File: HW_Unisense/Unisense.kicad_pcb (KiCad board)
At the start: 2 copper layers, 72 parts, among them J2 SW1, J3 SW2, J4 GeigerCounter, J5 WS2812, J6 LED1, J7 LED2, J8 LED3, P1 SM02B-NSHSS-TB(LF)(SN), Q1 BSN20, Q2 BSN20, Q3 BSN20, Q4 BSN20, Q5 AO3400A, Q6 AO3400A, Q7 AO3400A, Q8 IRLML6402TRPBF, SW1 K2-1102SP-C4SC-04, SW2 K2-1102SP-C4SC-04, SW3 K2-1102SP-C4SC-04, SW4 K2-1102SP-C4SC-04, U1 ESP32-S3-WROOM-1(N8R2), U2 S4B-PH-SM4-K-TB(LF)(SN), U3 LD1117S33TR, U4 TMP112xxDRL, U5 BME280, U6 BMP280, U7 VEML6040A3OG, U8 MCP73831T-2ATI/OT, U9 MAX17048G+T10

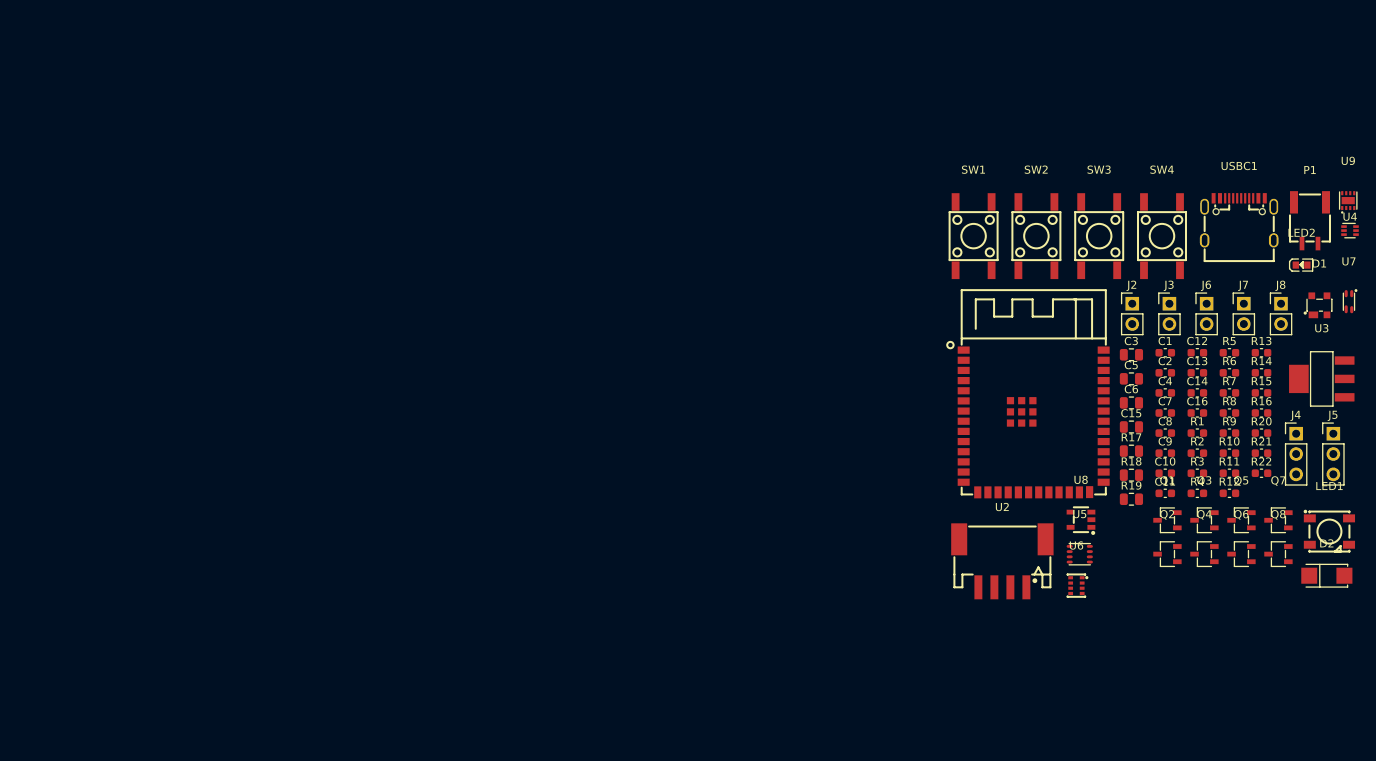
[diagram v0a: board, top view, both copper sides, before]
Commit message: add more sensors and arrange on multiple pages
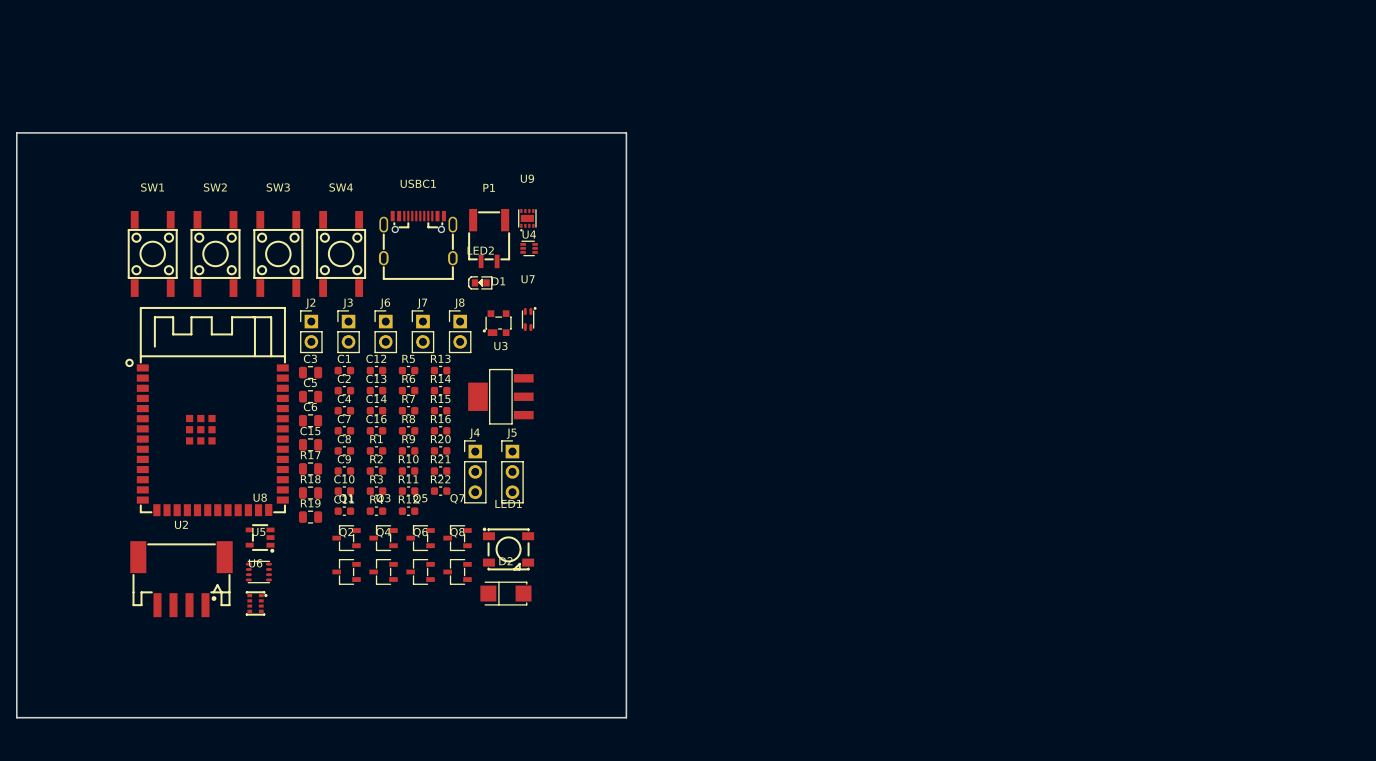
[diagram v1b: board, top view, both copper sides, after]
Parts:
- moved C1 102.6 mm to (150.3, 89.3)
- moved C10 102.6 mm to (150.3, 104.4)
- moved C11 102.6 mm to (150.3, 106.9)
- moved C12 102.6 mm to (154.4, 89.3)
- moved C13 102.6 mm to (154.4, 91.8)
- moved C14 102.6 mm to (154.4, 94.3)
- moved C16 102.6 mm to (154.4, 96.8)
- moved C2 102.6 mm to (150.3, 91.8)
- moved C4 102.6 mm to (150.3, 94.3)
- moved C7 102.6 mm to (150.3, 96.8)
- moved C8 102.6 mm to (150.3, 99.3)
- moved C9 102.6 mm to (150.3, 101.9)
- moved D1 102.6 mm to (169.6, 83.4)
- moved J2 102.6 mm to (146.2, 83.2)
- moved J5 102.6 mm to (171.4, 99.4)
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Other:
- board outline added: 76.2 x 73.1 mm

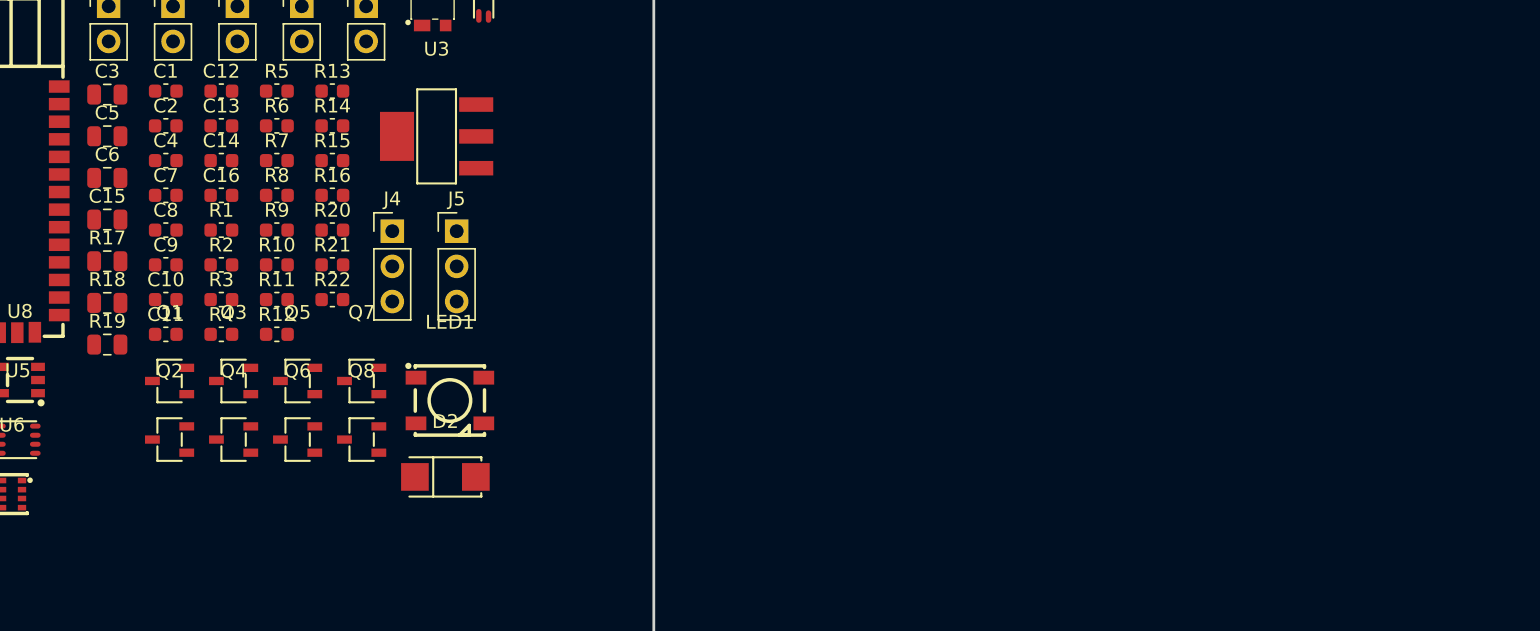
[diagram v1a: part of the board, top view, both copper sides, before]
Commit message: change power net names, as V8 handles them like a champ
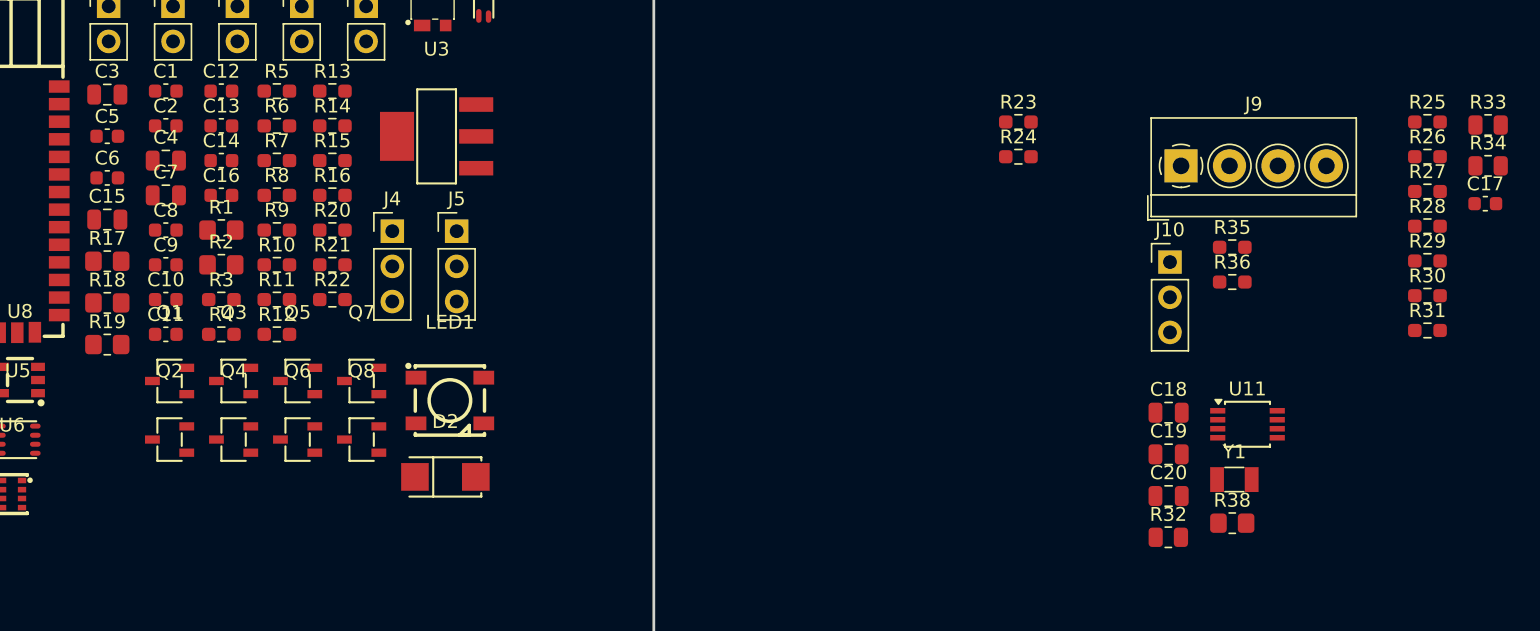
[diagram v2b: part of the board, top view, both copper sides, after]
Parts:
- added C17: 100n, Capacitor_SMD:C_0603_1608Metric, F.Cu at (245.7, 97.4)
- added C18: 1uF, Capacitor_SMD:C_0805_2012Metric, F.Cu at (222.8, 112.5)
- added C19: 100nF, Capacitor_SMD:C_0805_2012Metric, F.Cu at (222.8, 115.5)
- added C20: 100nF, Capacitor_SMD:C_0805_2012Metric, F.Cu at (222.8, 118.6)
- added J10: OneWire, Connector_PinHeader_2.54mm:PinHeader_1x03_P2.54mm_Vertical, F.Cu at (222.9, 101.7)
- added J9: RS485, TerminalBlock_4Ucon:TerminalBlock_4Ucon_1x04_P3.50mm_Horizontal, F.Cu at (223.7, 94.7)
- added R23: 100k, Resistor_SMD:R_0603_1608Metric_Pad0.98x0.95mm_HandSolder, F.Cu at (211.9, 91.5)
- added R24: 100k, Resistor_SMD:R_0603_1608Metric_Pad0.98x0.95mm_HandSolder, F.Cu at (211.9, 94.0)
- added R25: 100k, Resistor_SMD:R_0603_1608Metric_Pad0.98x0.95mm_HandSolder, F.Cu at (241.5, 91.5)
- added R26: 1k, Resistor_SMD:R_0603_1608Metric_Pad0.98x0.95mm_HandSolder, F.Cu at (241.5, 94.0)
- added R27: 1k, Resistor_SMD:R_0603_1608Metric_Pad0.98x0.95mm_HandSolder, F.Cu at (241.5, 96.6)
- added R28: 1k, Resistor_SMD:R_0603_1608Metric_Pad0.98x0.95mm_HandSolder, F.Cu at (241.5, 99.1)
- added R29: 1k, Resistor_SMD:R_0603_1608Metric_Pad0.98x0.95mm_HandSolder, F.Cu at (241.5, 101.6)
- added R30: 1k, Resistor_SMD:R_0603_1608Metric_Pad0.98x0.95mm_HandSolder, F.Cu at (241.5, 104.1)
- added R31: 1k, Resistor_SMD:R_0603_1608Metric_Pad0.98x0.95mm_HandSolder, F.Cu at (241.5, 106.6)
- added R32: 10k, Resistor_SMD:R_0805_2012Metric, F.Cu at (222.8, 121.5)
- added R33: 10k, Resistor_SMD:R_0805_2012Metric, F.Cu at (245.9, 91.8)
- added R34: 10k, Resistor_SMD:R_0805_2012Metric, F.Cu at (245.9, 94.7)
- added R35: 33k, Resistor_SMD:R_0603_1608Metric_Pad0.98x0.95mm_HandSolder, F.Cu at (227.4, 100.6)
- added R36: 1k, Resistor_SMD:R_0603_1608Metric_Pad0.98x0.95mm_HandSolder, F.Cu at (227.4, 103.1)
- added R38: 4R7, Resistor_SMD:R_0805_2012Metric_Pad1.20x1.40mm_HandSolder, F.Cu at (227.4, 120.5)
- added U11: PCF85263ATT, Package_SO:TSSOP-8_3x3mm_P0.65mm, F.Cu at (228.5, 113.4)
- added Y1: Crystal, Crystal:Crystal_SMD_3215-2Pin_3.2x1.5mm, F.Cu at (227.5, 117.4)
- C4, C7: value 100n -> 10u; footprint Capacitor_SMD:C_0603_1608Metric -> Capacitor_SMD:C_0805_2012Metric
- C5, C6: value 10u -> 100n; footprint Capacitor_SMD:C_0805_2012Metric -> Capacitor_SMD:C_0603_1608Metric
- R1, R2: footprint Capacitor_SMD:C_0603_1608Metric -> Resistor_SMD:R_0805_2012Metric_Pad1.20x1.40mm_HandSolder
- R10, R11, R13, R14, R20, R21, R22, R3, R4, R5, R6, R7, R8, R9: footprint Capacitor_SMD:C_0603_1608Metric -> Resistor_SMD:R_0603_1608Metric_Pad0.98x0.95mm_HandSolder
- R12, R16: value 1k -> 100k; footprint Capacitor_SMD:C_0603_1608Metric -> Resistor_SMD:R_0603_1608Metric_Pad0.98x0.95mm_HandSolder
- R15: value 1k -> 21k; footprint Capacitor_SMD:C_0603_1608Metric -> Resistor_SMD:R_0603_1608Metric_Pad0.98x0.95mm_HandSolder
- R17, R18, R19: footprint Capacitor_SMD:C_0805_2012Metric -> Resistor_SMD:R_0805_2012Metric_Pad1.20x1.40mm_HandSolder
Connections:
- C10 pad 1: SDA -> Net-(U6-VDD)
- C12 pad 1: Net-(U6-VDD) -> +VSW
- C13 pad 1: SDA -> +VSW
- C14 pad 2: SDA -> +VSW
- C2 pad 1: SDA -> +3.3V
- C3 pad 1: SDA -> +3.3V
- C6 pad 1: SDA -> +3.3V
- C7 pad 1: SDA -> +3.3V
- C8 pad 1: +5V -> Vdrive
- C9 pad 1: SDA -> +VSW
- J4 pad 2: +5V -> Vdrive
- J5 pad 1: +5V -> Vdrive
- LED1 pad 1: +5V -> Vdrive
- Q1 pad 1: SDA -> +VSW
- Q2 pad 1: SDA -> +VSW
- Q2 pad 2: Net-(Q2-S) -> SDA
- Q3 pad 1: SDA -> +VSW
- Q4 pad 1: SDA -> +VSW
- R10 pad 2: SDA -> +VSW
- R11 pad 2: +5V -> Vdrive
- R12 pad 1: SDA -> +3.3V
- R13 pad 2: SDA -> +VSW
- R14 pad 2: +5V -> Vdrive
- R16 pad 1: SDA -> +3.3V
- R17 pad 2: +5V -> Vdrive
- R18 pad 2: +5V -> Vdrive
- R19 pad 2: +5V -> Vdrive
- R3 pad 2: Net-(USBC1-CC1) -> Net-(USBC1-CC2)
- R4 pad 2: Net-(USBC1-CC2) -> Net-(USBC1-CC1)
- R5 pad 2: SDA -> +3.3V
- R6 pad 1: Net-(Q2-S) -> SCL
- R6 pad 2: SDA -> +VSW
- R7 pad 1: Net-(Q2-D) -> SDA
- R7 pad 2: Net-(JP1-C) -> +VSW
- R9 pad 1: SCL -> Net-(Q2-D)
- R9 pad 2: SDA -> Net-(JP1-C)
- U1 pad 10: unconnected-(U1-IO17-Pad10) -> RS485_TX
- U1 pad 11: unconnected-(U1-IO18-Pad11) -> RS485_RX
- U1 pad 12: unconnected-(U1-IO8-Pad12) -> ~{General_Reset}
- U1 pad 16: unconnected-(U1-IO46-Pad16) -> LED1
- U1 pad 17: WS2812_Data2 -> LED2
- U1 pad 18: LED1 -> LED3
- U1 pad 19: LED2 -> TFT_CS
- U1 pad 2: SDA -> +3.3V
- U1 pad 20: LED3 -> SPI0_MISO
- U1 pad 21: unconnected-(U1-IO13-Pad21) -> SPI0_MOSI
- U1 pad 22: unconnected-(U1-IO14-Pad22) -> SPI0_CLK
- U1 pad 31: unconnected-(U1-IO38-Pad31) -> OnWire_Data
- U1 pad 32: unconnected-(U1-IO39-Pad32) -> EnPower
- U1 pad 4: WS2812_Data1 -> unconnected-(U1-IO4-Pad4)
- U1 pad 6: unconnected-(U1-IO6-Pad6) -> RS485_EN
- U1 pad 7: unconnected-(U1-IO7-Pad7) -> WS2812_Data1
- U1 pad 8: unconnected-(U1-IO15-Pad8) -> WS2812_Data2
- U1 pad 9: unconnected-(U1-IO16-Pad9) -> TFT_DC
- U3 pad 2: SDA -> +3.3V
- U3 pad 4: SDA -> +3.3V
- U4 pad 5: SDA -> +VSW
- U5 pad 2: SDA -> +VSW
- U5 pad 6: SDA -> +VSW
- U5 pad 8: SDA -> +VSW
- U6 pad 2: SDA -> +VSW
- U7 pad 4: SDA -> +VSW
